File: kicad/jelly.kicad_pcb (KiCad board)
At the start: 2 copper layers, 59.9 x 32.9 mm, 29 parts, among them M1 PAGER_MOTOR, M2 PAGER_MOTOR, P1 CONN_01X01, P10 CONN_01X01, P11 CONN_01X01, P12 CONN_01X01, P13 CONN_01X01, P14 CONN_01X01, P15 CONN_01X01, P2 CONN_01X01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

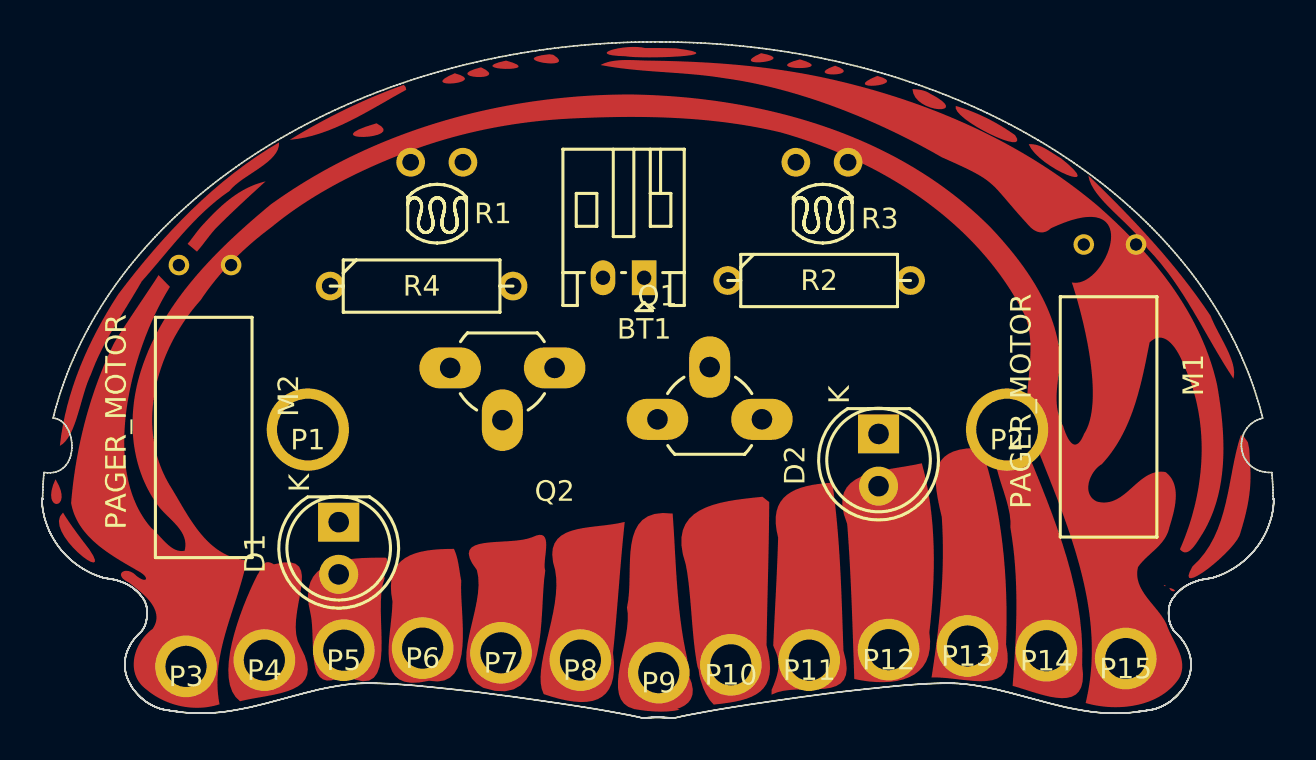
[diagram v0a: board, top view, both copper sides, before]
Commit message: Adjust position of right motor
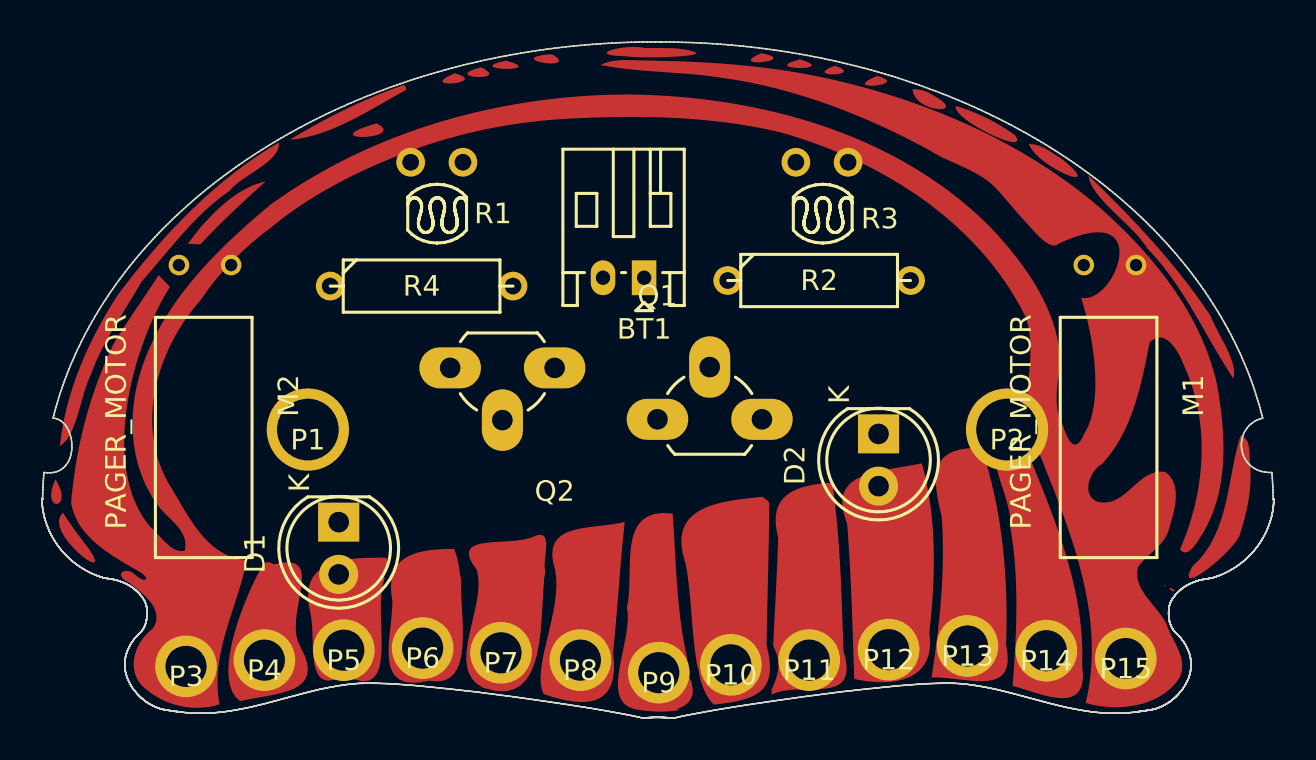
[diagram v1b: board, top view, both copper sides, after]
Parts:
- moved M1 1.00 mm to (172.0, 75.0)

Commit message: Play around with some routing
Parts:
- moved Q2 6.94 mm to (151.5, 82.5), turned to 0 degrees
- moved Q1 2.51 mm to (148.5, 80.5), turned to 180 degrees
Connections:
- P10 pad 1: GND -> Vout1
- P13 pad 1: Vout1 -> VCC
- P2 pad 1: Net-(P2-Pad1) -> VCC
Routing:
- net VCC: track 0.00 -> 23.5 mm
- net Vout2: track 0.00 -> 1.90 mm
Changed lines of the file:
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@@
 (kicad_pcb (version 20160815) (host pcbnew 4.1.0-alpha+201608271546+7097~46~ubuntu14.04.1-product)
   (general
-    (links 28)
-    (no_connects 28)
+    (links 29)
+    (no_connects 27)
     (area 119.662141 58.550827 180.412426 101.693013)
     (thickness 1.6)
     (drawings 0)
-    (tracks 0)
+    (tracks 12)
     (zones 0)
     (modules 29)
-    (nets 12)
+    (nets 11)
   )
   (page A4)
@@
   (net 7 "Net-(BT1-Pad1)")
   (net 8 "Net-(P1-Pad1)")
-  (net 9 "Net-(P2-Pad1)")
-  (net 10 "Net-(D1-Pad1)")
-  (net 11 "Net-(D2-Pad1)")
+  (net 9 "Net-(D1-Pad1)")
+  (net 10 "Net-(D2-Pad1)")
   (net_class Default "This is the default net class."
     (clearance 0.2)
@@
     (add_net "Net-(D2-Pad1)")
     (add_net "Net-(P1-Pad1)")
-    (add_net "Net-(P2-Pad1)")
     (add_net "Net-(Q1-Pad2)")
     (add_net "Net-(Q2-Pad2)")
@@
     )
     (pad 1 thru_hole rect (at 0 0) (size 2 1.9) (drill 1.00076) (layers *.Cu *.Mask F.SilkS)
-      (net 10 "Net-(D1-Pad1)"))
+      (net 9 "Net-(D1-Pad1)"))
     (pad 2 thru_hole circle (at 2.54 0 270) (size 1.9 1.9) (drill 1.00076) (layers *.Cu *.Mask F.SilkS)
       (net 2 Vout1))
@@
     )
     (pad 1 thru_hole rect (at 0 0) (size 2 1.9) (drill 1.00076) (layers *.Cu *.Mask F.SilkS)
-      (net 11 "Net-(D2-Pad1)"))
+      (net 10 "Net-(D2-Pad1)"))
     (pad 2 thru_hole circle (at 2.54 0 270) (size 1.9 1.9) (drill 1.00076) (layers *.Cu *.Mask F.SilkS)
       (net 3 Vout2))
@@
     (fp_line (start -3.81 -0.635) (end -3.175 -1.27) (layer F.SilkS) (width 0.15))
     (pad 1 thru_hole circle (at -4.445 0) (size 1.397 1.397) (drill 0.8128) (layers *.Cu *.Mask F.SilkS)
-      (net 10 "Net-(D1-Pad1)"))
+      (net 9 "Net-(D1-Pad1)"))
     (pad 2 thru_hole circle (at 4.445 0) (size 1.397 1.397) (drill 0.8128) (layers *.Cu *.Mask F.SilkS)
       (net 1 VCC))
@@
     (fp_line (start -3.81 -0.635) (end -3.175 -1.27) (layer F.SilkS) (width 0.15))
     (pad 1 thru_hole circle (at -4.445 0) (size 1.397 1.397) (drill 0.8128) (layers *.Cu *.Mask F.SilkS)
-      (net 11 "Net-(D2-Pad1)"))
+      (net 10 "Net-(D2-Pad1)"))
     (pad 2 thru_hole circle (at 4.445 0) (size 1.397 1.397) (drill 0.8128) (layers *.Cu *.Mask F.SilkS)
       (net 1 VCC))
@@
   )
   (module KiCad/TO_SOT_Packages_THT.pretty:TO-92_Rugged (layer F.Cu)
-    (at 145 80 180)
+    (at 151.46 82.54)
     (descr "TO-92 rugged, leads molded, wide, drill 1mm (see NXP sot054_po.pdf)")
     (tags "to-92 sc-43 sc-43a sot54 PA33 transistor")
-    (fp_text reference Q2 (at 0 -6 180) (layer F.SilkS)
+    (fp_text reference Q2 (at 0 -6) (layer F.SilkS)
       (effects (font (size 1 1) (thickness 0.15)))
     )
-    (fp_text value 2N7000 (at 0 3 180) (layer F.Fab)
+    (fp_text value 2N7000 (at 0 3) (layer F.Fab)
       (effects (font (size 1 1) (thickness 0.15)))
     )
@@
     (fp_line (start -1.75 -4.3) (end 6.85 -4.3) (layer F.CrtYd) (width 0.05))
     (fp_line (start 6.85 1.95) (end 6.85 -4.3) (layer F.CrtYd) (width 0.05))
-    (pad 2 thru_hole oval (at 2.54 -2.54 270) (size 2.99974 1.99898) (drill 1) (layers *.Cu *.Mask F.SilkS)
+    (pad 2 thru_hole oval (at 2.54 -2.54 90) (size 2.99974 1.99898) (drill 1) (layers *.Cu *.Mask F.SilkS)
       (net 5 "Net-(Q2-Pad2)"))
-    (pad 1 thru_hole oval (at 0 0 270) (size 1.99898 2.99974) (drill 1) (layers *.Cu *.Mask F.SilkS)
+    (pad 1 thru_hole oval (at 0 0 90) (size 1.99898 2.99974) (drill 1) (layers *.Cu *.Mask F.SilkS)
       (net 6 GND))
-    (pad 3 thru_hole oval (at 5.08 0 270) (size 1.99898 2.99974) (drill 1) (layers *.Cu *.Mask F.SilkS)
+    (pad 3 thru_hole oval (at 5.08 0 90) (size 1.99898 2.99974) (drill 1) (layers *.Cu *.Mask F.SilkS)
       (net 3 Vout2))
     (model TO_SOT_Packages_THT.3dshapes/TO-92_Rugged.wrl
@@
     )
     (pad 1 thru_hole circle (at 0 0) (size 4 4) (drill 3) (layers *.Cu *.Mask)
-      (net 9 "Net-(P2-Pad1)"))
+      (net 1 VCC))
   )
   (module custom:hole2 (layer F.Cu)
@@
     )
     (pad 1 thru_hole circle (at 0 0) (size 3 3) (drill 2) (layers *.Cu *.Mask)
-      (net 2 Vout1))
+      (net 1 VCC))
   )
   (module custom:hole2 (layer F.Cu)
@@
     )
     (pad 1 thru_hole circle (at 0 0) (size 3 3) (drill 2) (layers *.Cu *.Mask)
-      (net 6 GND))
+      (net 2 Vout1))
   )
   (module custom:hole2 (layer F.Cu)
@@
   )
   (module KiCad/TO_SOT_Packages_THT.pretty:TO-92_Rugged (layer F.Cu)
-    (at 150 82.5)
+    (at 148.54 80.46 180)
     (descr "TO-92 rugged, leads molded, wide, drill 1mm (see NXP sot054_po.pdf)")
     (tags "to-92 sc-43 sc-43a sot54 PA33 transistor")
-    (fp_text reference Q1 (at 0 -6) (layer F.SilkS)
+    (fp_text reference Q1 (at 0 -6 180) (layer F.SilkS)
       (effects (font (size 1 1) (thickness 0.15)))
     )
-    (fp_text value 2N7000 (at 0 3) (layer F.Fab)
+    (fp_text value 2N7000 (at 0 3 180) (layer F.Fab)
       (effects (font (size 1 1) (thickness 0.15)))
     )
@@
     (fp_line (start -1.75 -4.3) (end 6.85 -4.3) (layer F.CrtYd) (width 0.05))
     (fp_line (start 6.85 1.95) (end 6.85 -4.3) (layer F.CrtYd) (width 0.05))
-    (pad 2 thru_hole oval (at 2.54 -2.54 90) (size 2.99974 1.99898) (drill 1) (layers *.Cu *.Mask F.SilkS)
+    (pad 2 thru_hole oval (at 2.54 -2.54 270) (size 2.99974 1.99898) (drill 1) (layers *.Cu *.Mask F.SilkS)
       (net 4 "Net-(Q1-Pad2)"))
-    (pad 1 thru_hole oval (at 0 0 90) (size 1.99898 2.99974) (drill 1) (layers *.Cu *.Mask F.SilkS)
+    (pad 1 thru_hole oval (at 0 0 270) (size 1.99898 2.99974) (drill 1) (layers *.Cu *.Mask F.SilkS)
       (net 6 GND))
-    (pad 3 thru_hole oval (at 5.08 0 90) (size 1.99898 2.99974) (drill 1) (layers *.Cu *.Mask F.SilkS)
+    (pad 3 thru_hole oval (at 5.08 0 270) (size 1.99898 2.99974) (drill 1) (layers *.Cu *.Mask F.SilkS)
       (net 2 Vout1))
     (model TO_SOT_Packages_THT.3dshapes/TO-92_Rugged.wrl
@@
       (xy 24.885017 10.694285)) (layer F.Cu) (width 0))
   )
+  (segment (start 163.899 80.5688) (end 164.9476 80.5688) (width 0.25) (layer F.Cu) (net 1))
+  (segment (start 164.9476 80.5688) (end 167.1066 82.7278) (width 0.25) (layer F.Cu) (net 1))
+  (segment (start 167.1066 82.7278) (end 167.1066 83.0326) (width 0.25) (layer F.Cu) (net 1))
+  (segment (start 167.1066 83.0326) (end 167.0558 83.0834) (width 0.25) (layer F.Cu) (net 1))
+  (segment (start 167.0558 83.0834) (end 167 83) (width 0.25) (layer F.Cu) (net 1))
+  (segment (start 163.899 84.4478) (end 165.0746 85.6234) (width 0.25) (layer F.Cu) (net 1))
+  (segment (start 165.0746 85.6234) (end 165.0746 93.5228) (width 0.25) (layer F.Cu) (net 1))
+  (segment (start 163.899 77.343) (end 163.899 80.5688) (width 0.25) (layer F.Cu) (net 1))
+  (segment (start 163.899 80.5688) (end 163.899 84.4478) (width 0.25) (layer F.Cu) (net 1))
+  (segment (start 162.306 75.75) (end 163.899 77.343) (width 0.25) (layer F.Cu) (net 1))
+  (segment (start 156.54 82.54) (end 156.54 83.78949) (width 0.25) (layer F.Cu) (net 3))
+  (segment (start 156.54 83.78949) (end 157 84.24949) (width 0.25) (layer F.Cu) (net 3))
 )

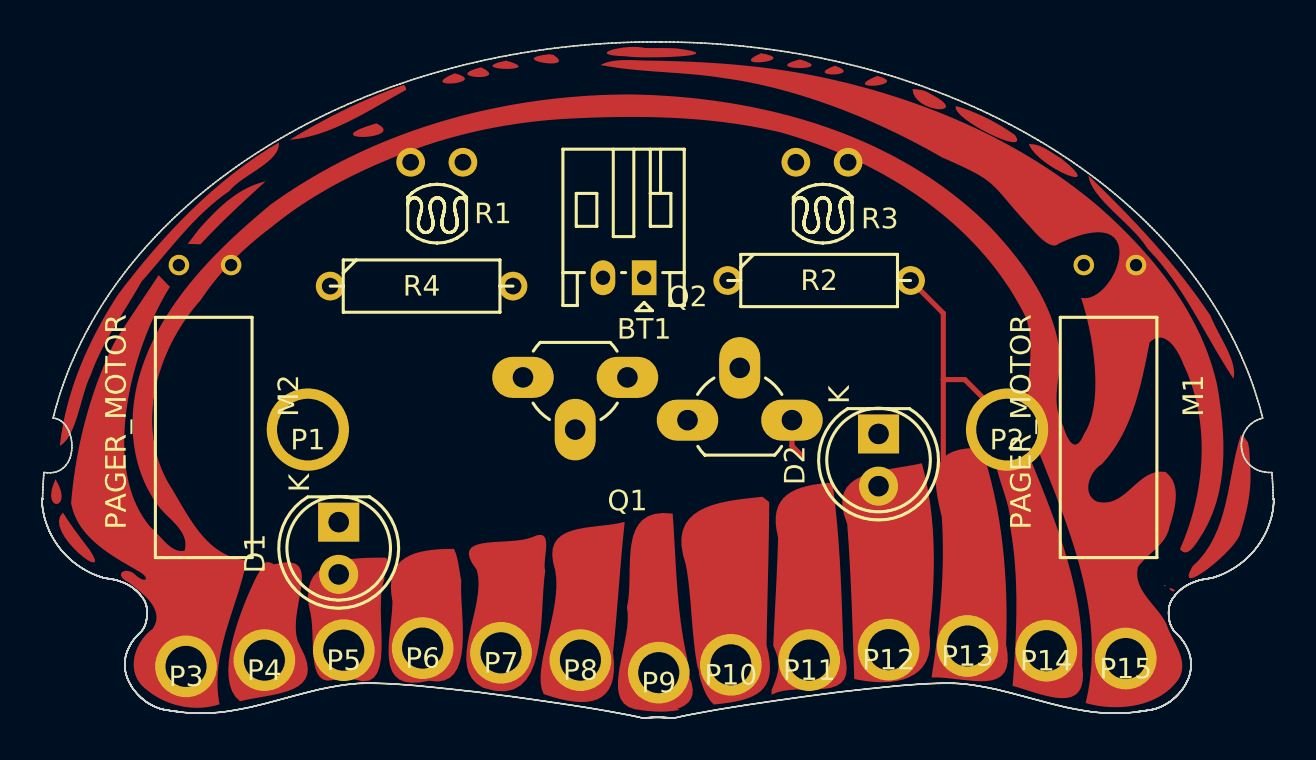
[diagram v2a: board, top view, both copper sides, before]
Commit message: Switch to CR2450 battery holder
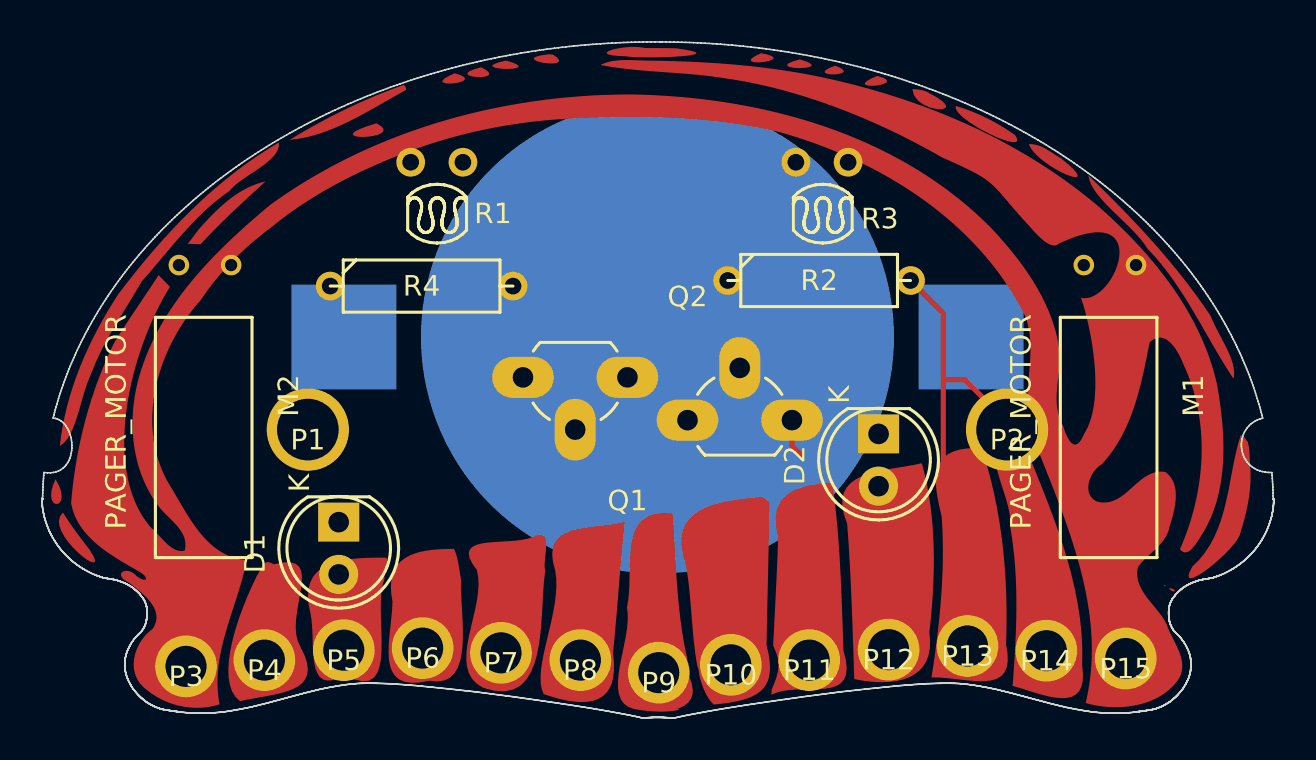
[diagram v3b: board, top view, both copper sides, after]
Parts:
- BT1: footprint KiCad/Connectors_JST.pretty:JST_PH_S2B-PH-K_02x2.00mm_Angled -> custom:cr2450_holder; moved to B.Cu
- moved BT1 2.96 mm to (150.0, 78.5)
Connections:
- P10 pad 1: Vout1 -> Vout2
- P11 pad 1: Vout1 -> Vout2
- P12 pad 1: Vout1 -> Vout2
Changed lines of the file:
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@@
 (kicad_pcb (version 20160815) (host pcbnew 4.1.0-alpha+201608271546+7097~46~ubuntu14.04.1-product)
   (general
-    (links 29)
-    (no_connects 27)
+    (links 30)
+    (no_connects 26)
     (area 119.662141 58.550827 180.412426 101.693013)
     (thickness 1.6)
@@
     (add_net Vout2)
   )
+  (module custom:cr2450_holder (layer B.Cu)
+    (at 150 78.5 180)
+    (fp_text reference BT1 (at 0 -0.5 180) (layer B.SilkS)
+      (effects (font (size 1 1) (thickness 0.15)) (justify mirror))
+    )
+    (fp_text value BATTERY (at 0 0.5 180) (layer B.Fab)
+      (effects (font (size 1 1) (thickness 0.15)) (justify mirror))
+    )
+    (fp_arc (start -9 8) (end -12 8) (angle -180) (layer B.SilkS) (width 0.15))
+    (fp_arc (start 9 8) (end 6 8) (angle -180) (layer B.SilkS) (width 0.15))
+    (fp_line (start -12 8) (end -12 -7) (layer B.SilkS) (width 0.15))
+    (fp_line (start -12 -7) (end -4 -14) (layer B.SilkS) (width 0.15))
+    (fp_line (start -4 -14) (end 4 -14) (layer B.SilkS) (width 0.15))
+    (fp_line (start 4 -14) (end 12 -7) (layer B.SilkS) (width 0.15))
+    (fp_line (start 12 -7) (end 12 8) (layer B.SilkS) (width 0.15))
+    (pad 1 smd rect (at -15.25 0 180) (size 5.1 5.1) (layers B.Cu B.Paste B.Mask)
+      (net 7 "Net-(BT1-Pad1)"))
+    (pad 1 smd rect (at 15.25 0 180) (size 5.1 5.1) (layers B.Cu B.Paste B.Mask)
+      (net 7 "Net-(BT1-Pad1)"))
+    (pad 2 smd circle (at 0 0 180) (size 23 23) (layers B.Cu B.Paste B.Mask)
+      (net 6 GND))
+  )
   (module KiCad/LEDs.pretty:LED-5MM (layer F.Cu)
     (at 134.5 87.5 270)
@@
     )
   )
-  (module KiCad/Connectors_JST.pretty:JST_PH_S2B-PH-K_02x2.00mm_Angled (layer F.Cu)
-    (at 149.352 75.6158 180)
-    (descr http://www.jst-mfg.com/product/pdf/eng/ePH.pdf)
-    (tags "connector jst ph")
-    (fp_text reference BT1 (at 0 -2.5 180) (layer F.SilkS)
-      (effects (font (size 1 1) (thickness 0.15)))
-    )
-    (fp_text value BATTERY (at 1 7.5 180) (layer F.Fab)
-      (effects (font (size 1 1) (thickness 0.15)))
-    )
-    (fp_line (start 0.5 6.25) (end 0.5 2) (layer F.SilkS) (width 0.15))
-    (fp_line (start 0.5 2) (end 1.5 2) (layer F.SilkS) (width 0.15))
-    (fp_line (start 1.5 2) (end 1.5 6.25) (layer F.SilkS) (width 0.15))
-    (fp_line (start -0.9 0.25) (end -1.25 0.25) (layer F.SilkS) (width 0.15))
-    (fp_line (start -1.25 0.25) (end -1.25 -1.35) (layer F.SilkS) (width 0.15))
-    (fp_line (start -1.25 -1.35) (end -1.95 -1.35) (layer F.SilkS) (width 0.15))
-    (fp_line (start -1.95 -1.35) (end -1.95 6.25) (layer F.SilkS) (width 0.15))
-    (fp_line (start -1.95 6.25) (end 3.95 6.25) (layer F.SilkS) (width 0.15))
-    (fp_line (start 3.95 6.25) (end 3.95 -1.35) (layer F.SilkS) (width 0.15))
-    (fp_line (start 3.95 -1.35) (end 3.25 -1.35) (layer F.SilkS) (width 0.15))
-    (fp_line (start 3.25 -1.35) (end 3.25 0.25) (layer F.SilkS) (width 0.15))
-    (fp_line (start 3.25 0.25) (end 2.9 0.25) (layer F.SilkS) (width 0.15))
-    (fp_line (start 0 -1.2) (end -0.4 -1.6) (layer F.SilkS) (width 0.15))
-    (fp_line (start -0.4 -1.6) (end 0.4 -1.6) (layer F.SilkS) (width 0.15))
-    (fp_line (start 0.4 -1.6) (end 0 -1.2) (layer F.SilkS) (width 0.15))
-    (fp_line (start -1.95 0.25) (end -1.25 0.25) (layer F.SilkS) (width 0.15))
-    (fp_line (start 3.95 0.25) (end 3.25 0.25) (layer F.SilkS) (width 0.15))
-    (fp_line (start -1.3 2.5) (end -1.3 4.1) (layer F.SilkS) (width 0.15))
-    (fp_line (start -1.3 4.1) (end -0.3 4.1) (layer F.SilkS) (width 0.15))
-    (fp_line (start -0.3 4.1) (end -0.3 2.5) (layer F.SilkS) (width 0.15))
-    (fp_line (start -0.3 2.5) (end -1.3 2.5) (layer F.SilkS) (width 0.15))
-    (fp_line (start 3.3 2.5) (end 3.3 4.1) (layer F.SilkS) (width 0.15))
-    (fp_line (start 3.3 4.1) (end 2.3 4.1) (layer F.SilkS) (width 0.15))
-    (fp_line (start 2.3 4.1) (end 2.3 2.5) (layer F.SilkS) (width 0.15))
-    (fp_line (start 2.3 2.5) (end 3.3 2.5) (layer F.SilkS) (width 0.15))
-    (fp_line (start -0.3 4.1) (end -0.3 6.25) (layer F.SilkS) (width 0.15))
-    (fp_line (start -0.8 4.1) (end -0.8 6.25) (layer F.SilkS) (width 0.15))
-    (fp_line (start 0.9 0.25) (end 1.1 0.25) (layer F.SilkS) (width 0.15))
-    (fp_line (start -2.45 6.75) (end -2.45 -1.85) (layer F.CrtYd) (width 0.05))
-    (fp_line (start -2.45 -1.85) (end 4.45 -1.85) (layer F.CrtYd) (width 0.05))
-    (fp_line (start 4.45 -1.85) (end 4.45 6.75) (layer F.CrtYd) (width 0.05))
-    (fp_line (start 4.45 6.75) (end -2.45 6.75) (layer F.CrtYd) (width 0.05))
-    (pad 1 thru_hole rect (at 0 0 180) (size 1.2 1.7) (drill 0.7) (layers *.Cu *.Mask F.SilkS)
-      (net 7 "Net-(BT1-Pad1)"))
-    (pad 2 thru_hole oval (at 2 0 180) (size 1.2 1.7) (drill 0.7) (layers *.Cu *.Mask F.SilkS)
-      (net 6 GND))
-  )
   (module custom:pager_motor_custom (layer F.Cu)
     (at 128 75 180)
@@
     )
     (pad 1 thru_hole circle (at 0 0) (size 3 3) (drill 2) (layers *.Cu *.Mask)
-      (net 2 Vout1))
+      (net 3 Vout2))
   )
   (module custom:hole2 (layer F.Cu)
@@
     )
     (pad 1 thru_hole circle (at 0 0) (size 3 3) (drill 2) (layers *.Cu *.Mask)
-      (net 2 Vout1))
+      (net 3 Vout2))
   )
   (module custom:hole2 (layer F.Cu)
@@
     )
     (pad 1 thru_hole circle (at 0 0) (size 3 3) (drill 2) (layers *.Cu *.Mask)
-      (net 2 Vout1))
+      (net 3 Vout2))
   )
   (module custom:hole2 (layer F.Cu)
@@
       (xy 24.885017 10.694285)) (layer F.Cu) (width 0))
   )
-  (segment (start 163.899 80.5688) (end 164.9476 80.5688) (width 0.25) (layer F.Cu) (net 1))
   (segment (start 164.9476 80.5688) (end 167.1066 82.7278) (width 0.25) (layer F.Cu) (net 1))
   (segment (start 167.1066 82.7278) (end 167.1066 83.0326) (width 0.25) (layer F.Cu) (net 1))
   (segment (start 167.1066 83.0326) (end 167.0558 83.0834) (width 0.25) (layer F.Cu) (net 1))
   (segment (start 167.0558 83.0834) (end 167 83) (width 0.25) (layer F.Cu) (net 1))
-  (segment (start 163.899 84.4478) (end 165.0746 85.6234) (width 0.25) (layer F.Cu) (net 1))
   (segment (start 165.0746 85.6234) (end 165.0746 93.5228) (width 0.25) (layer F.Cu) (net 1))
-  (segment (start 163.899 77.343) (end 163.899 80.5688) (width 0.25) (layer F.Cu) (net 1))
-  (segment (start 163.899 80.5688) (end 163.899 84.4478) (width 0.25) (layer F.Cu) (net 1))
   (segment (start 162.306 75.75) (end 163.899 77.343) (width 0.25) (layer F.Cu) (net 1))
+  (segment (start 163.899 80.5688) (end 164.9476 80.5688) (width 0.25) (layer F.Cu) (net 1))
+  (segment (start 163.899 84.4478) (end 165.0746 85.6234) (width 0.25) (layer F.Cu) (net 1))
+  (segment (start 163.899 80.5688) (end 163.899 84.4478) (width 0.25) (layer F.Cu) (net 1))
+  (segment (start 163.899 77.343) (end 163.899 80.5688) (width 0.25) (layer F.Cu) (net 1))
   (segment (start 156.54 82.54) (end 156.54 83.78949) (width 0.25) (layer F.Cu) (net 3))
   (segment (start 156.54 83.78949) (end 157 84.24949) (width 0.25) (layer F.Cu) (net 3))
